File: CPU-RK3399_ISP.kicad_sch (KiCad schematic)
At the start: 1 part, among them U1 RK3399

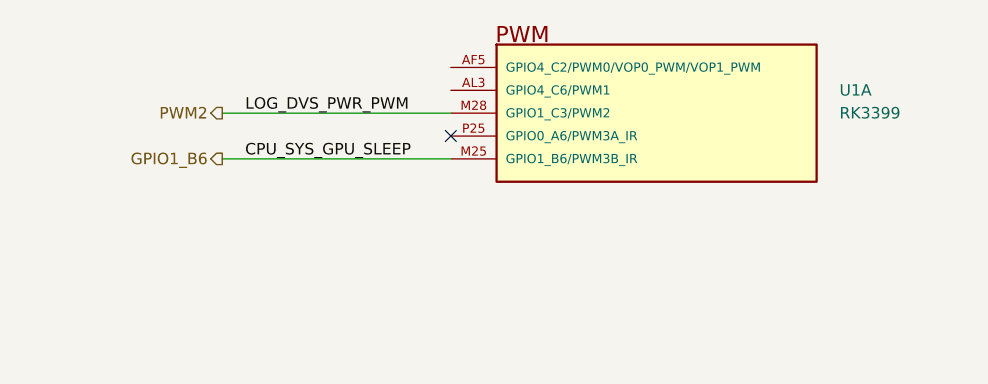
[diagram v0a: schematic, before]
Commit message: update schematic
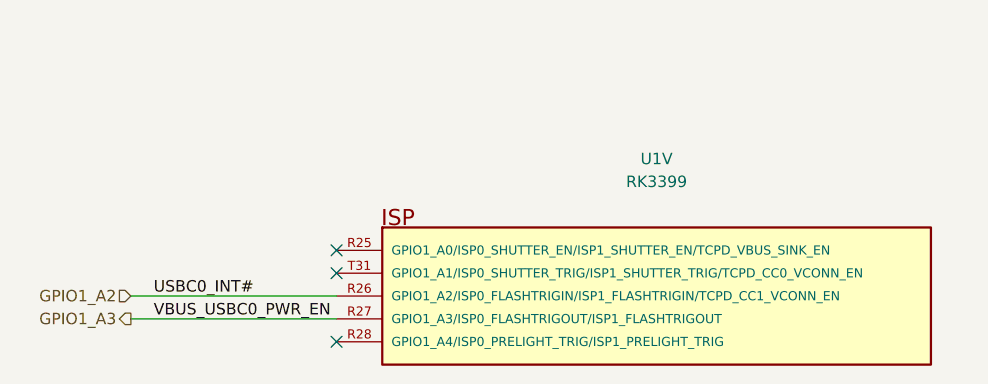
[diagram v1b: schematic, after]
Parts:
- removed U1: RK3399, footprints:BGA828C65P31X31_2100X2100X161, symbol component_library:System On Chip (SoC)/RK3399
- added U1: RK3399, footprints:BGA828C65P31X31_2100X2100X161, symbol component_library:System On Chip (SoC)/RK3399
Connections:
- new net GPIO1_A2: U1.R26 (GPIO1_A2/ISP0_FLASHTRIGIN/ISP1_FLASHTRIGIN/TCPD_CC1_VCONN_EN)
- new net GPIO1_A3: U1.R27 (GPIO1_A3/ISP0_FLASHTRIGOUT/ISP1_FLASHTRIGOUT)
- no-connect marks 1 -> 3
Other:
- title: (none) -> CPU-RK3399 ISP Controller
